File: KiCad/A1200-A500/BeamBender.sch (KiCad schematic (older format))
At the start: 46 parts, among them J1 4-1734742-0, J2 HDMI_A_1.4, J3 STX-3501-3N, J4 Phoenix_Contact, U1 LM1117-3.3, U3 ADV7513BSWZ, X1 Abracon ASE-27.000MHZ-L-R-T, X2 Oscillator_7.0x5.0mm

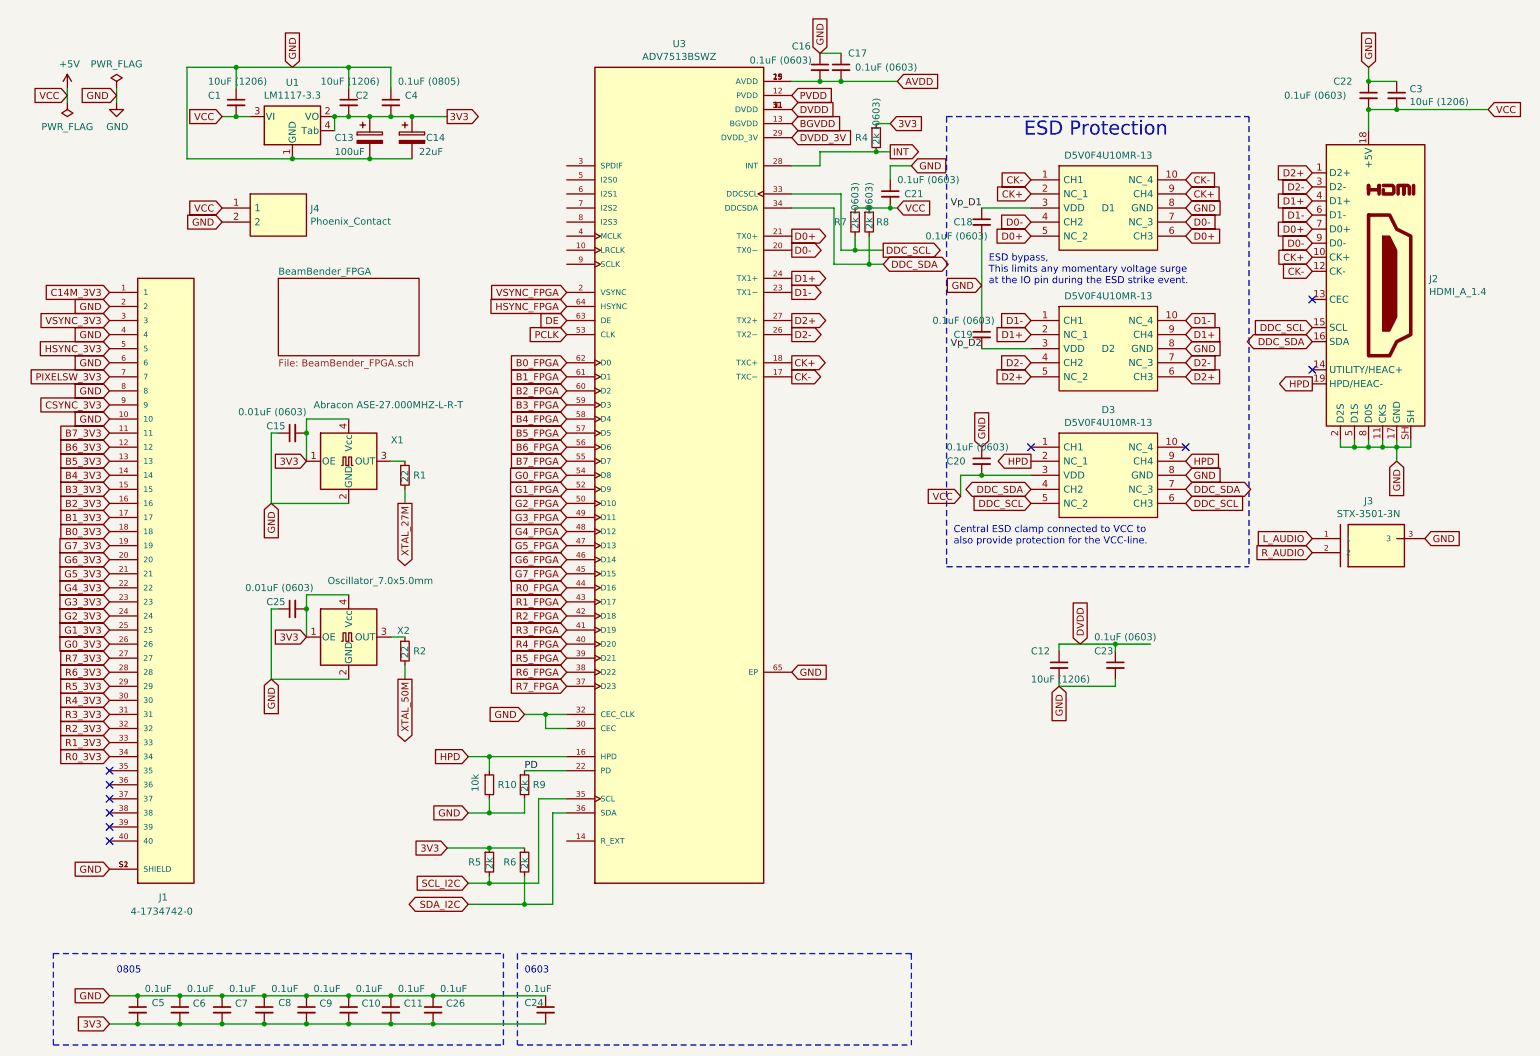
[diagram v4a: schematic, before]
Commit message: Added a 1.8V LDO (MCP1702T-1802E_CB) in SOT-23 for powering the ADV7513 with 1.8V (DVDD,AVDD,PVDD,BGVDD)
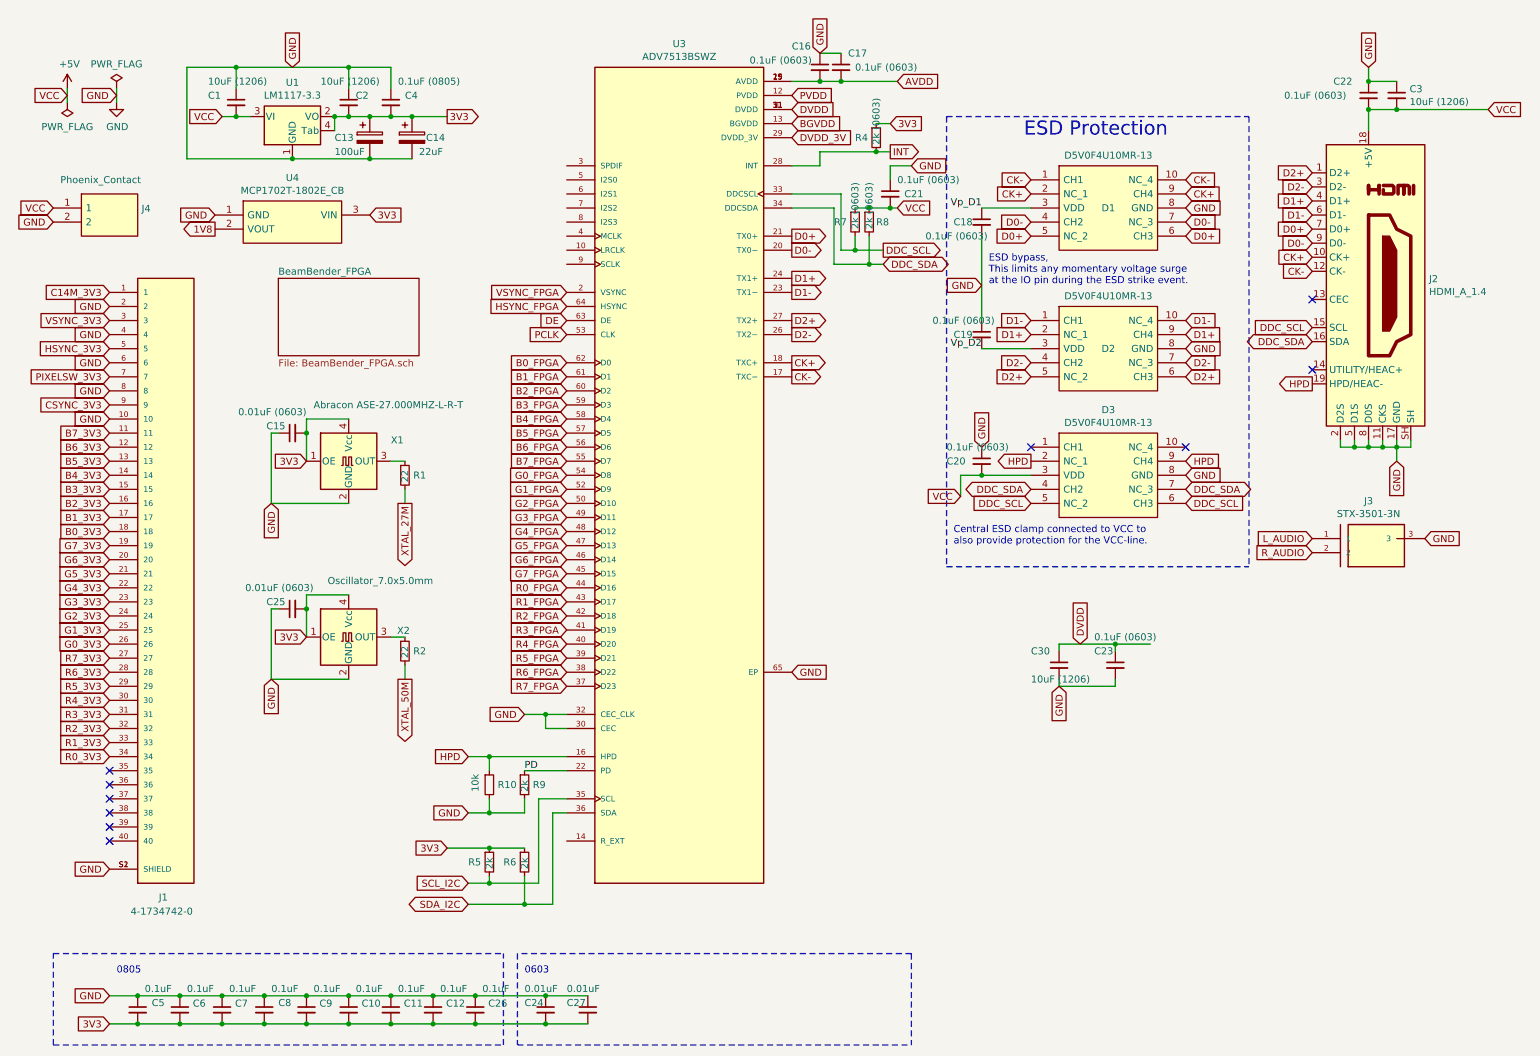
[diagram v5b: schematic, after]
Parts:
- added C26: 0.1uF, Capacitor_SMD:C_0805_2012Metric_Pad1.18x1.45mm_HandSolder, symbol Device:C_Small
- added C27: 0.01uF, Capacitor_SMD:C_0603_1608Metric_Pad1.08x0.95mm_HandSolder, symbol Device:C_Small
- added U4: MCP1702T-1802E_CB, Package_TO_SOT_SMD:SOT-23_Handsoldering, symbol BeamBender:MCP1702T-1802E_CB
- C24: value 0.1uF -> 0.01uF
- renumbered C26 to C12, C12 to C30
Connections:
- net 3V3: now also C26.2, C27.2, U4.3 (VIN)
- net GND: now also C26.1, C27.1, U4.1 (GND)
- new net 1V8: U4.2 (VOUT)
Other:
- moved on the sheet: J4
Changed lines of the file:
@@
 L BeamBender:Phoenix_Contact J4
 U 1 1 654E9506
-P 2350 1850
-F 0 "J4" H 2578 1896 50  0000 L CNN
-F 1 "Phoenix_Contact" H 2578 1805 50  0000 L CNN
-F 2 "BeamBender:Phoenix_Contact" H 2600 2000 50  0001 L CNN
-F 3 "" H 2600 1900 50  0001 L CNN
-	1    2350 1850
-	1    0    0    -1
-$EndComp
-Text GLabel 1950 1800 0    50   Input ~ 0
+P 1150 1850
+F 0 "J4" H 1378 1896 50  0000 L CNN
+F 1 "Phoenix_Contact" H 800 2100 50  0000 L CNN
+F 2 "BeamBender:Phoenix_Contact" H 1400 2000 50  0001 L CNN
+F 3 "" H 1400 1900 50  0001 L CNN
+	1    1150 1850
+	1    0    0    -1
+$EndComp
+Text GLabel 750  1800 0    50   Input ~ 0
 VCC
-Text GLabel 1950 1900 0    50   Input ~ 0
+Text GLabel 750  1900 0    50   Input ~ 0
 GND
 $Comp
@@
 AVDD
 $Comp
-L Device:C_Small C12
+L Device:C_Small C30
 U 1 1 657943FC
 P 7900 5050
-F 0 "C12" H 7700 5150 50  0000 L CNN
+F 0 "C30" H 7700 5150 50  0000 L CNN
 F 1 "10uF (1206)" H 7700 4950 50  0000 L CNN
 F 2 "Capacitor_SMD:C_1206_3216Metric_Pad1.33x1.80mm_HandSolder" H 7900 5050 50  0001 C CNN
@@
 P 4250 7500
 F 0 "C24" H 4100 7550 50  0000 L CNN
-F 1 "0.1uF" H 4100 7650 50  0000 L CNN
+F 1 "0.01uF" H 4100 7650 50  0000 L CNN
 F 2 "Capacitor_SMD:C_0603_1608Metric_Pad1.08x0.95mm_HandSolder" H 4250 7500 50  0001 C CNN
 F 3 "~" H 4250 7500 50  0001 C CNN
@@
 	2300 4650 2350 4650
 $Comp
-L Device:C_Small C26
+L Device:C_Small C12
 U 1 1 6591CDE3
 P 3450 7500
-F 0 "C26" H 3542 7546 50  0000 L CNN
+F 0 "C12" H 3542 7546 50  0000 L CNN
 F 1 "0.1uF" H 3500 7650 50  0000 L CNN
 F 2 "Capacitor_SMD:C_0805_2012Metric_Pad1.18x1.45mm_HandSolder" H 3450 7500 50  0001 C CNN
@@
 	750  7750 3950 7750
 Wire Wire Line
-	3450 7400 4250 7400
-Wire Wire Line
-	3450 7600 4250 7600
+	3450 7400 3750 7400
+Wire Wire Line
+	3450 7600 3750 7600
 Wire Notes Line
 	4050 7100 4050 7750
@@
 Wire Notes Line
 	6850 7100 4050 7100
+$Comp
+L Device:C_Small C26
+U 1 1 659AF7E7
+P 3750 7500
+F 0 "C26" H 3842 7546 50  0000 L CNN
+F 1 "0.1uF" H 3800 7650 50  0000 L CNN
+F 2 "Capacitor_SMD:C_0805_2012Metric_Pad1.18x1.45mm_HandSolder" H 3750 7500 50  0001 C CNN
+F 3 "~" H 3750 7500 50  0001 C CNN
+	1    3750 7500
+	1    0    0    -1
+$EndComp
+Connection ~ 3750 7400
+Wire Wire Line
+	3750 7400 4250 7400
+Connection ~ 3750 7600
+Wire Wire Line
+	3750 7600 4250 7600
+$Comp
+L Device:C_Small C27
+U 1 1 659B84AB
+P 4550 7500
+F 0 "C27" H 4400 7550 50  0000 L CNN
+F 1 "0.01uF" H 4400 7650 50  0000 L CNN
+F 2 "Capacitor_SMD:C_0603_1608Metric_Pad1.08x0.95mm_HandSolder" H 4550 7500 50  0001 C CNN
+F 3 "~" H 4550 7500 50  0001 C CNN
+	1    4550 7500
+	1    0    0    -1
+$EndComp
+Wire Wire Line
+	4250 7400 4550 7400
+Connection ~ 4250 7400
+Wire Wire Line
+	4250 7600 4550 7600
+Connection ~ 4250 7600
+$Comp
+L BeamBender:MCP1702T-1802E_CB U4
+U 1 1 659F5664
+P 2450 1900
+F 0 "U4" H 2450 2215 50  0000 C CNN
+F 1 "MCP1702T-1802E_CB" H 2450 2124 50  0000 C CNN
+F 2 "Package_TO_SOT_SMD:SOT-23_Handsoldering" H 2850 2050 50  0001 L CNN
+F 3 "" H 2850 1950 50  0001 L CNN
+	1    2450 1900
+	1    0    0    -1
+$EndComp
+Text GLabel 3000 1850 2    50   Input ~ 0
+3V3
+Text GLabel 1900 1850 0    50   Input ~ 0
+GND
+Text GLabel 1900 1950 0    50   Output ~ 0
+1V8
 $EndSCHEMATC

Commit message: More power routing done
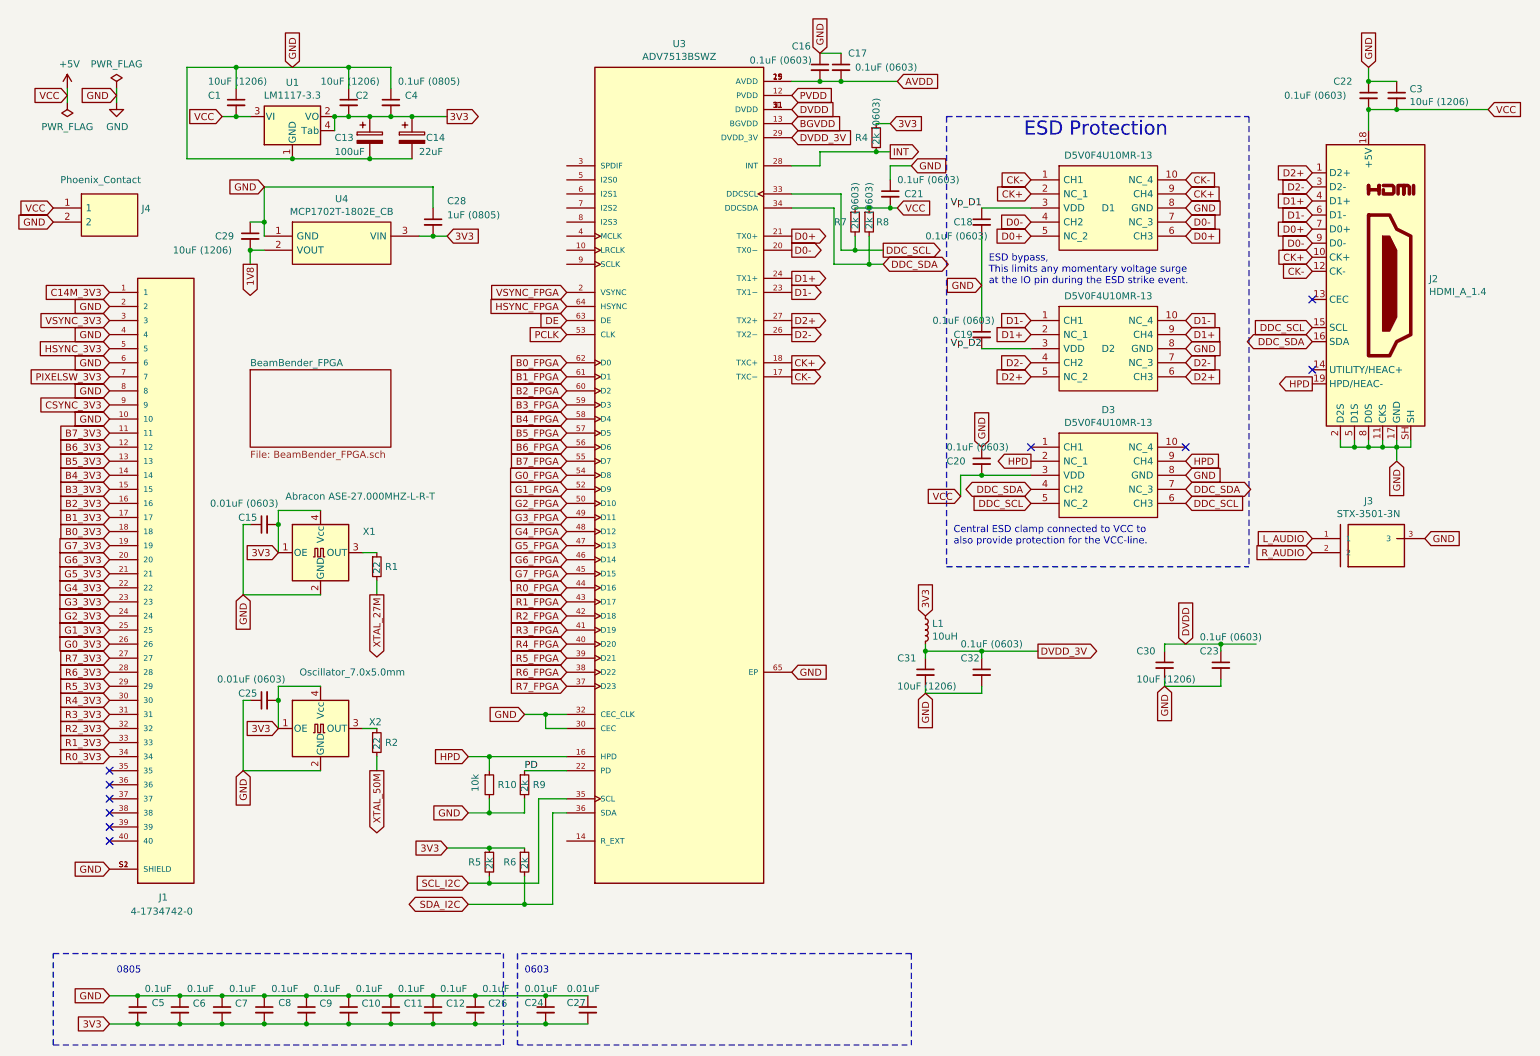
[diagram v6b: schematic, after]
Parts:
- added C28: 1uF (0805), Capacitor_SMD:C_0805_2012Metric_Pad1.18x1.45mm_HandSolder, symbol Device:C_Small
- added C29, C31: 10uF (1206), Capacitor_SMD:C_1206_3216Metric_Pad1.33x1.80mm_HandSolder, symbol Device:C_Small
- added C32: 0.1uF (0603), Capacitor_SMD:C_0603_1608Metric_Pad1.08x0.95mm_HandSolder, symbol Device:C_Small
- added L1: 10uH, Capacitor_SMD:C_0805_2012Metric_Pad1.18x1.45mm_HandSolder, symbol Device:L_Small
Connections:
- net 1V8: now also C29.2
- net 3V3: now also C28.2, L1.1
- net DVDD_3V: now also C31.1, C32.1, L1.2
- net GND: now also C28.1, C29.1, C31.2, C32.2
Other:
- moved on the sheet: C15, C23, C25, C30, R1, R2, U4, X1, X2
